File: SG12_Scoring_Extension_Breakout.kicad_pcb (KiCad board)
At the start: 2 copper layers, 95 x 55 mm, 23 parts, among them J1 RJ45, J2 Barrel_Jack_MountingPin, J3 Barrel_Jack_MountingPin, J4 Barrel_Jack_MountingPin, J5 Barrel_Jack_MountingPin, J6 Barrel_Jack_MountingPin, J8 Conn_02x08_Odd_Even, Q1 IRF4905, Q2 IRF4905, Q3 IRF4905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

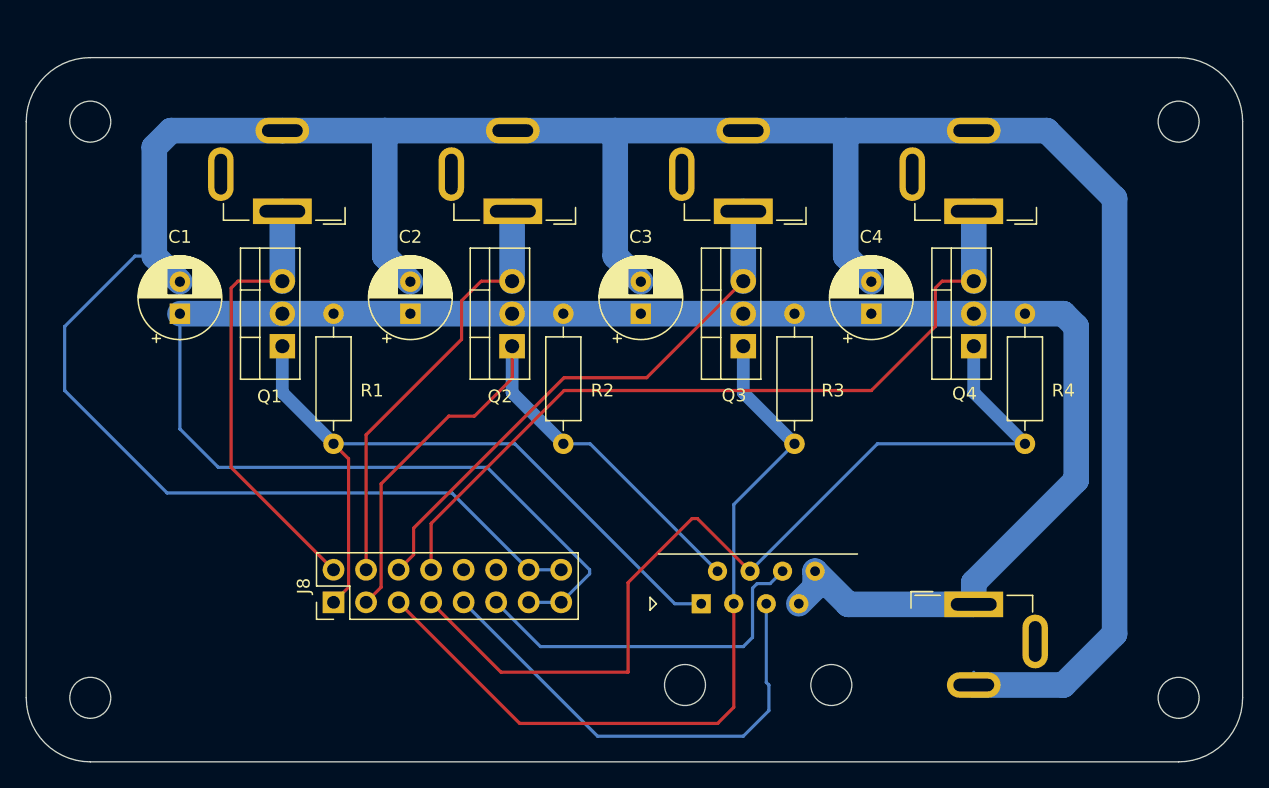
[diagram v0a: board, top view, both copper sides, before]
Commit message: Added silkscreen text
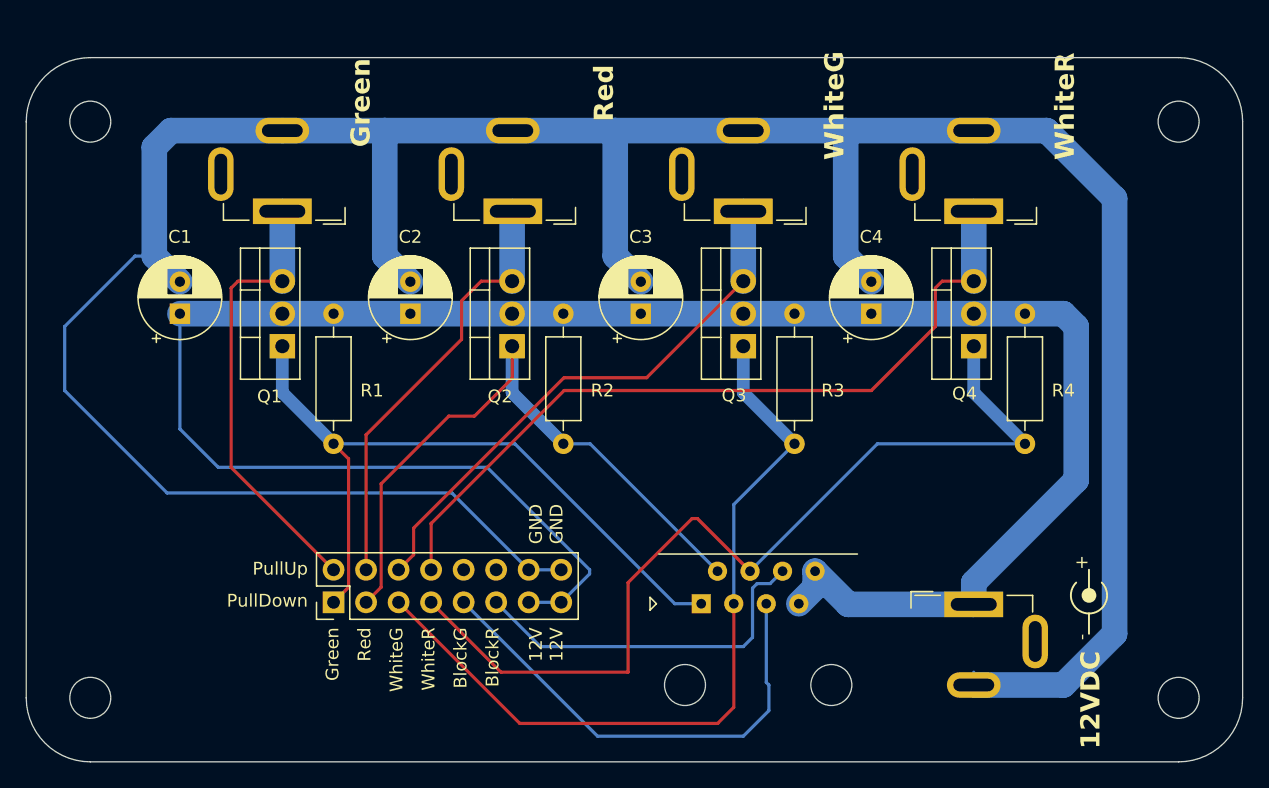
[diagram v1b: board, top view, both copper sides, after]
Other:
- board text added: "+"
- board text added: "-"
- board text added: "12V 12V"
- board text added: "12VDC"
- board text added: "BlockG"
- board text added: "BlockR"
- board text added: "GND GND"
- board text added: "Green"
- board text added: "PullDown"
- board text added: "PullUp"
- board text added: "Red"
- board text added: "WhiteG"
- board text added: "WhiteR"
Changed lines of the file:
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@@
       (outputformat 1)
       (mirror false)
-      (drillshape 1)
+      (drillshape 0)
       (scaleselection 1)
-      (outputdirectory "")
+      (outputdirectory "manufacturing/")
     )
   )
@@
     (property "ki_keywords" "connector")
     (attr through_hole)
-    (fp_text reference "J8" (at 1.27 -2.33 90) (layer "F.SilkS")
+    (fp_text reference "J8" (at 1.27 -2.33 90) (layer "F.SilkS") hide
         (effects (font (size 1 1) (thickness 0.15)))
     )
@@
     (pad "" np_thru_hole circle (at 0 0) (size 3.2 3.2) (drill 3.2) (layers "*.Cu" "*.Mask"))
   )
+  (gr_circle (center 199 120) (end 199.5 120)
+    (stroke (width 0.15) (type solid)) (fill solid) (layer "F.SilkS"))
+  (gr_arc (start 200 119) (mid 199 121.414214) (end 198 119)
+    (stroke (width 0.15) (type default)) (layer "F.SilkS"))
+  (gr_line (start 199 120) (end 199 118)
+    (stroke (width 0.15) (type default)) (layer "F.SilkS"))
+  (gr_line (start 199 121.414214) (end 199 123)
+    (stroke (width 0.15) (type default)) (layer "F.SilkS"))
   (gr_line (start 206 78) (end 121 78)
     (stroke (width 0.1) (type default)) (layer "Edge.Cuts"))
@@
   (gr_arc (start 121 133) (mid 117.464466 131.535534) (end 116 128)
     (stroke (width 0.1) (type default)) (layer "Edge.Cuts"))
+  (gr_text "PullDown" (at 138 121) (layer "F.SilkS")
+    (effects (font (size 1 1) (thickness 0.15)) (justify right bottom))
+  )
+  (gr_text "Red" (at 143 122.5 90) (layer "F.SilkS")
+    (effects (font (size 1 1) (thickness 0.15)) (justify right bottom))
+  )
+  (gr_text "12V\n12V" (at 158 122.5 90) (layer "F.SilkS")
+    (effects (font (size 1 1) (thickness 0.15)) (justify right bottom))
+  )
+  (gr_text "PullUp" (at 138 118.5) (layer "F.SilkS")
+    (effects (font (size 1 1) (thickness 0.15)) (justify right bottom))
+  )
+  (gr_text "+" (at 199 118 90) (layer "F.SilkS")
+    (effects (font (size 1 1) (thickness 0.15)) (justify left bottom))
+  )
+  (gr_text "BlockG" (at 150.5 122.5 90) (layer "F.SilkS")
+    (effects (font (size 1 1) (thickness 0.15)) (justify right bottom))
+  )
+  (gr_text "WhiteR" (at 198 86 90) (layer "F.SilkS")
+    (effects (font (size 1.5 1.5) (thickness 0.3) bold) (justify left bottom))
+  )
+  (gr_text "WhiteG" (at 180 86 90) (layer "F.SilkS")
+    (effects (font (size 1.5 1.5) (thickness 0.3) bold) (justify left bottom))
+  )
+  (gr_text "-" (at 199 123 90) (layer "F.SilkS")
+    (effects (font (size 1 1) (thickness 0.15)) (justify right bottom))
+  )
+  (gr_text "GND\nGND" (at 158 116 90) (layer "F.SilkS")
+    (effects (font (size 1 1) (thickness 0.15)) (justify left bottom))
+  )
+  (gr_text "BlockR" (at 153 122.5 90) (layer "F.SilkS")
+    (effects (font (size 1 1) (thickness 0.15)) (justify right bottom))
+  )
+  (gr_text "WhiteR" (at 148 122.5 90) (layer "F.SilkS")
+    (effects (font (size 1 1) (thickness 0.15)) (justify right bottom))
+  )
+  (gr_text "12VDC" (at 200 132 90) (layer "F.SilkS")
+    (effects (font (size 1.5 1.5) (thickness 0.3) bold) (justify left bottom))
+  )
+  (gr_text "Green" (at 143 85 90) (layer "F.SilkS")
+    (effects (font (size 1.5 1.5) (thickness 0.3) bold) (justify left bottom))
+  )
+  (gr_text "Red" (at 162 83 90) (layer "F.SilkS")
+    (effects (font (size 1.5 1.5) (thickness 0.3) bold) (justify left bottom))
+  )
+  (gr_text "Green" (at 140.5 122.5 90) (layer "F.SilkS")
+    (effects (font (size 1 1) (thickness 0.15)) (justify right bottom))
+  )
+  (gr_text "WhiteG" (at 145.5 122.5 90) (layer "F.SilkS")
+    (effects (font (size 1 1) (thickness 0.15)) (justify right bottom))
+  )
   (segment (start 141.175 109.335) (end 140 108.16) (width 0.25) (layer "F.Cu") (net 1))
   (segment (start 141.175 119.365) (end 141.175 109.335) (width 0.25) (layer "F.Cu") (net 1))

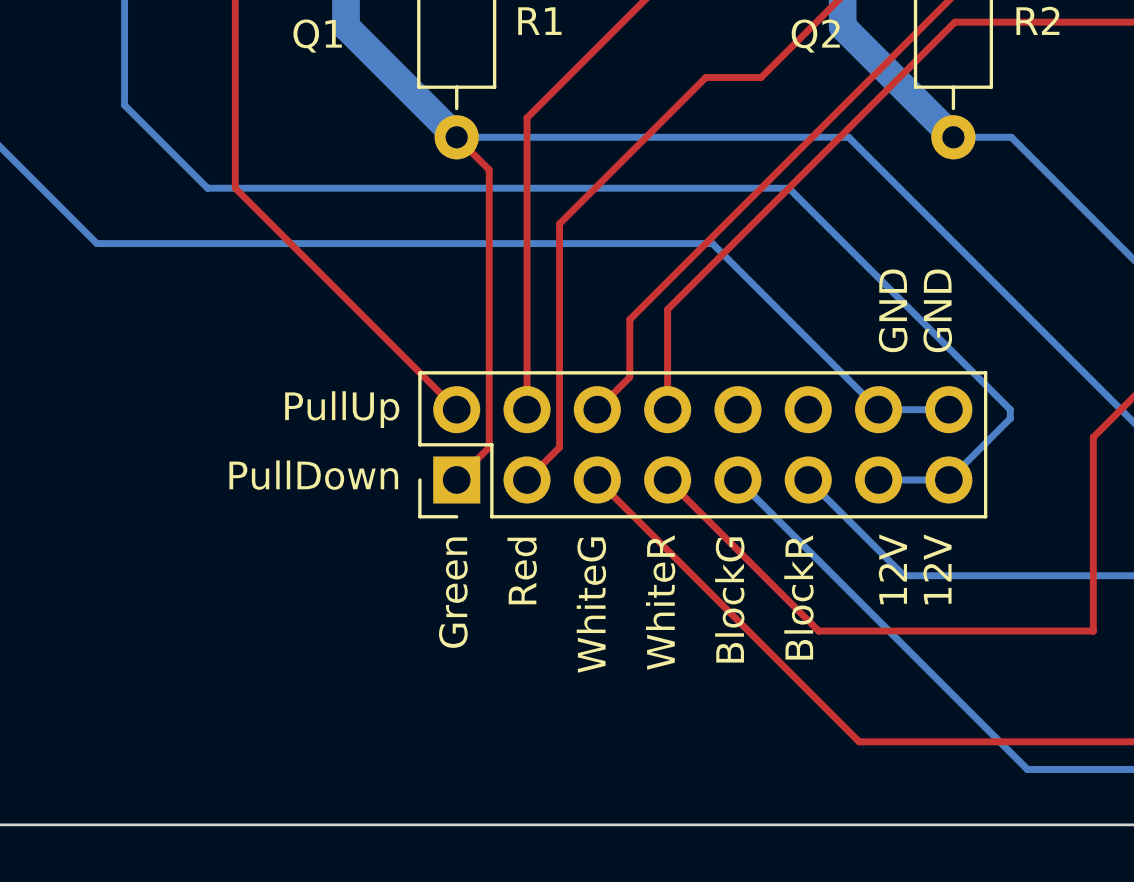
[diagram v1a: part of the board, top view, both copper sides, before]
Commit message: More silkscreen
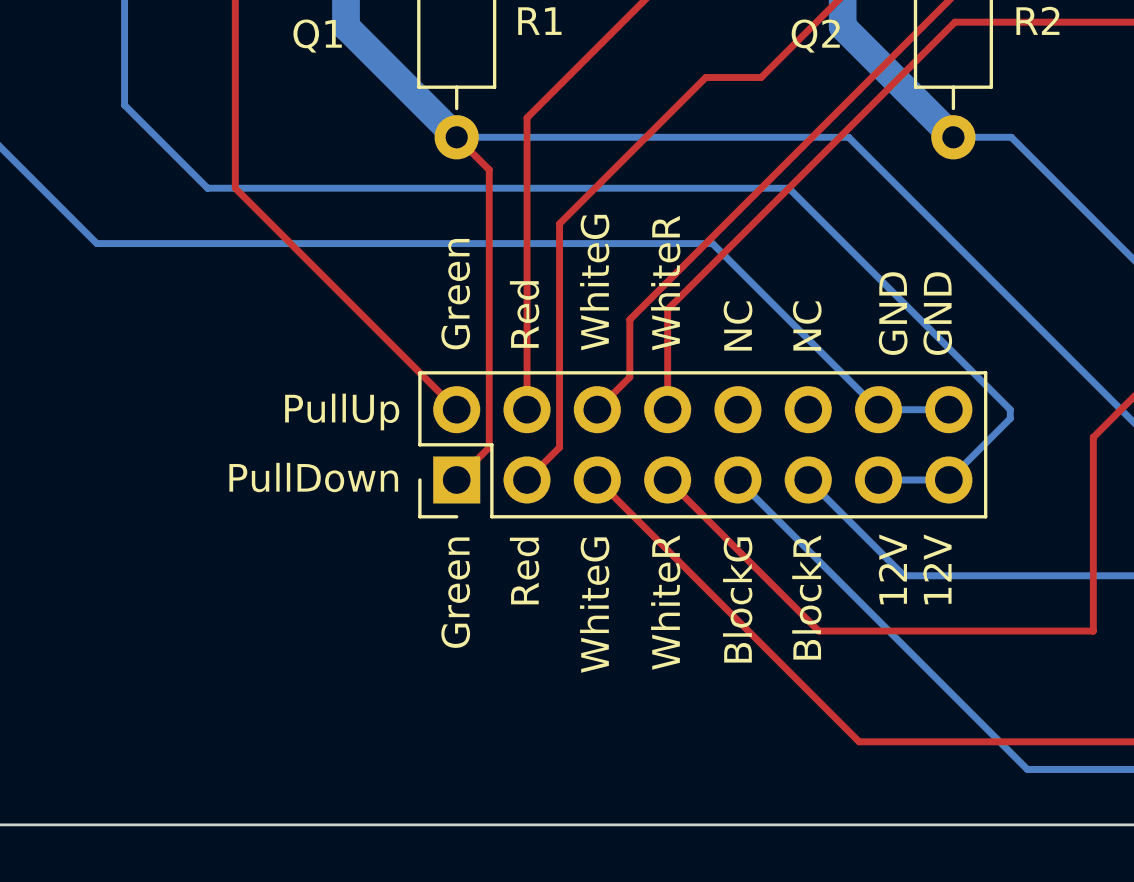
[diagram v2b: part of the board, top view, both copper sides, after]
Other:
- board text added: "NC"
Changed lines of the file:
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@@
   (gr_arc (start 121 133) (mid 117.464466 131.535534) (end 116 128)
     (stroke (width 0.1) (type default)) (layer "Edge.Cuts"))
-  (gr_text "PullDown" (at 138 121) (layer "F.SilkS")
-    (effects (font (size 1 1) (thickness 0.15)) (justify right bottom))
+  (gr_text "NC" (at 150.2 116 90) (layer "F.SilkS")
+    (effects (font (size 1 1) (thickness 0.15)) (justify left))
   )
-  (gr_text "Red" (at 143 122.5 90) (layer "F.SilkS")
-    (effects (font (size 1 1) (thickness 0.15)) (justify right bottom))
+  (gr_text "WhiteG" (at 145.034 115.9 90) (layer "F.SilkS")
+    (effects (font (size 1 1) (thickness 0.15)) (justify left))
+  )
+  (gr_text "PullDown" (at 138 120.5) (layer "F.SilkS")
+    (effects (font (size 1 1) (thickness 0.15)) (justify right))
+  )
+  (gr_text "NC" (at 152.7 116 90) (layer "F.SilkS")
+    (effects (font (size 1 1) (thickness 0.15)) (justify left))
+  )
+  (gr_text "Red" (at 142.5 122.5 90) (layer "F.SilkS")
+    (effects (font (size 1 1) (thickness 0.15)) (justify right))
   )
   (gr_text "12V\n12V" (at 158 122.5 90) (layer "F.SilkS")
     (effects (font (size 1 1) (thickness 0.15)) (justify right bottom))
   )
-  (gr_text "PullUp" (at 138 118.5) (layer "F.SilkS")
-    (effects (font (size 1 1) (thickness 0.15)) (justify right bottom))
+  (gr_text "PullUp" (at 138 118) (layer "F.SilkS")
+    (effects (font (size 1 1) (thickness 0.15)) (justify right))
   )
   (gr_text "+" (at 199 118 90) (layer "F.SilkS")
     (effects (font (size 1 1) (thickness 0.15)) (justify left bottom))
   )
-  (gr_text "BlockG" (at 150.5 122.5 90) (layer "F.SilkS")
-    (effects (font (size 1 1) (thickness 0.15)) (justify right bottom))
+  (gr_text "BlockG" (at 150.2 122.5 90) (layer "F.SilkS")
+    (effects (font (size 1 1) (thickness 0.15)) (justify right))
   )
   (gr_text "WhiteR" (at 198 86 90) (layer "F.SilkS")
     (effects (font (size 1.5 1.5) (thickness 0.3) bold) (justify left bottom))
+  )
+  (gr_text "Green" (at 140 115.9 90) (layer "F.SilkS")
+    (effects (font (size 1 1) (thickness 0.15)) (justify left))
+  )
+  (gr_text "WhiteR" (at 147.6 115.9 90) (layer "F.SilkS")
+    (effects (font (size 1 1) (thickness 0.15)) (justify left))
   )
   (gr_text "WhiteG" (at 180 86 90) (layer "F.SilkS")
@@
     (effects (font (size 1 1) (thickness 0.15)) (justify right bottom))
   )
-  (gr_text "GND\nGND" (at 158 116 90) (layer "F.SilkS")
+  (gr_text "GND\nGND" (at 158 116.1 90) (layer "F.SilkS")
     (effects (font (size 1 1) (thickness 0.15)) (justify left bottom))
   )
-  (gr_text "BlockR" (at 153 122.5 90) (layer "F.SilkS")
-    (effects (font (size 1 1) (thickness 0.15)) (justify right bottom))
+  (gr_text "BlockR" (at 152.7 122.5 90) (layer "F.SilkS")
+    (effects (font (size 1 1) (thickness 0.15)) (justify right))
   )
-  (gr_text "WhiteR" (at 148 122.5 90) (layer "F.SilkS")
-    (effects (font (size 1 1) (thickness 0.15)) (justify right bottom))
+  (gr_text "Red" (at 142.5 115.9 90) (layer "F.SilkS")
+    (effects (font (size 1 1) (thickness 0.15)) (justify left))
+  )
+  (gr_text "WhiteR" (at 147.6 122.5 90) (layer "F.SilkS")
+    (effects (font (size 1 1) (thickness 0.15)) (justify right))
   )
   (gr_text "12VDC" (at 200 132 90) (layer "F.SilkS")
@@
     (effects (font (size 1.5 1.5) (thickness 0.3) bold) (justify left bottom))
   )
-  (gr_text "Green" (at 140.5 122.5 90) (layer "F.SilkS")
-    (effects (font (size 1 1) (thickness 0.15)) (justify right bottom))
+  (gr_text "Green" (at 140 122.5 90) (layer "F.SilkS")
+    (effects (font (size 1 1) (thickness 0.15)) (justify right))
   )
-  (gr_text "WhiteG" (at 145.5 122.5 90) (layer "F.SilkS")
-    (effects (font (size 1 1) (thickness 0.15)) (justify right bottom))
+  (gr_text "WhiteG" (at 145.034 122.5 90) (layer "F.SilkS")
+    (effects (font (size 1 1) (thickness 0.15)) (justify right))
   )
   (segment (start 141.175 109.335) (end 140 108.16) (width 0.25) (layer "F.Cu") (net 1))

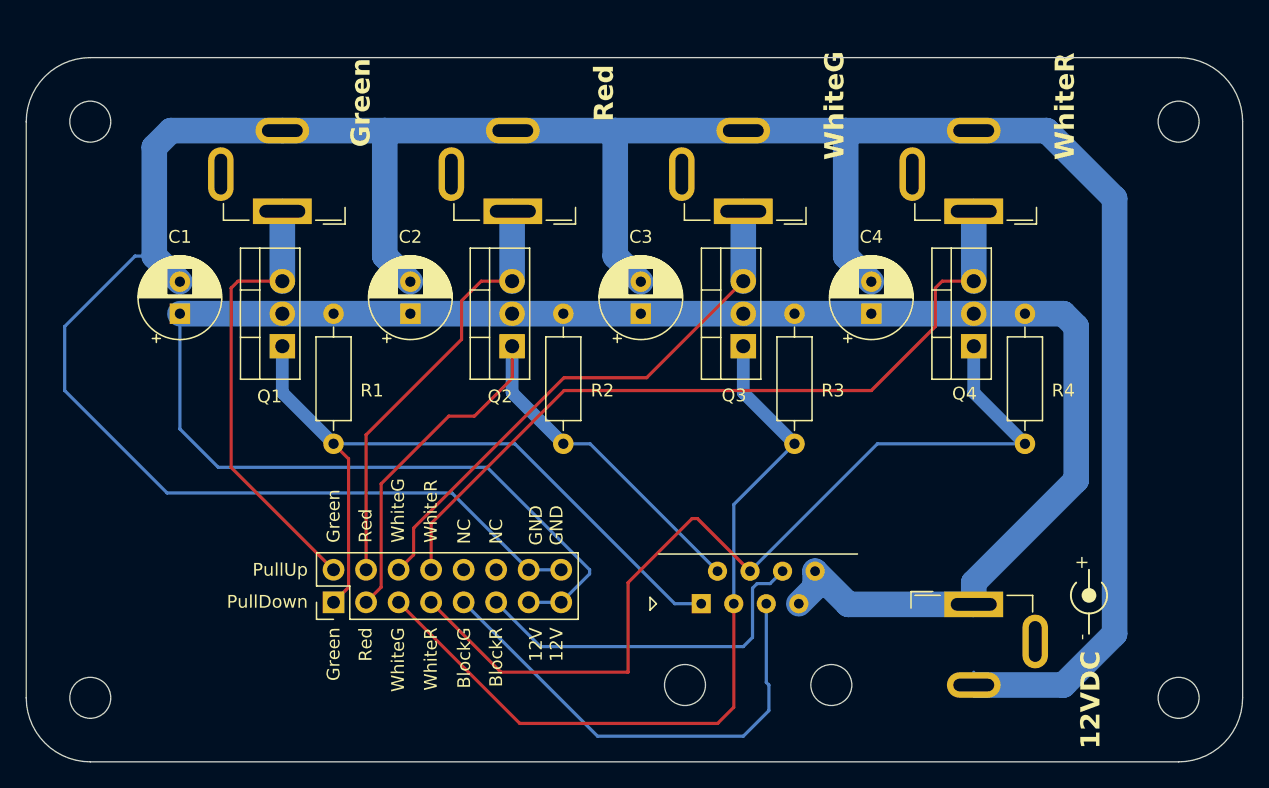
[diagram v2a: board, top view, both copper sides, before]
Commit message: Updated routing and RJ45 footprint
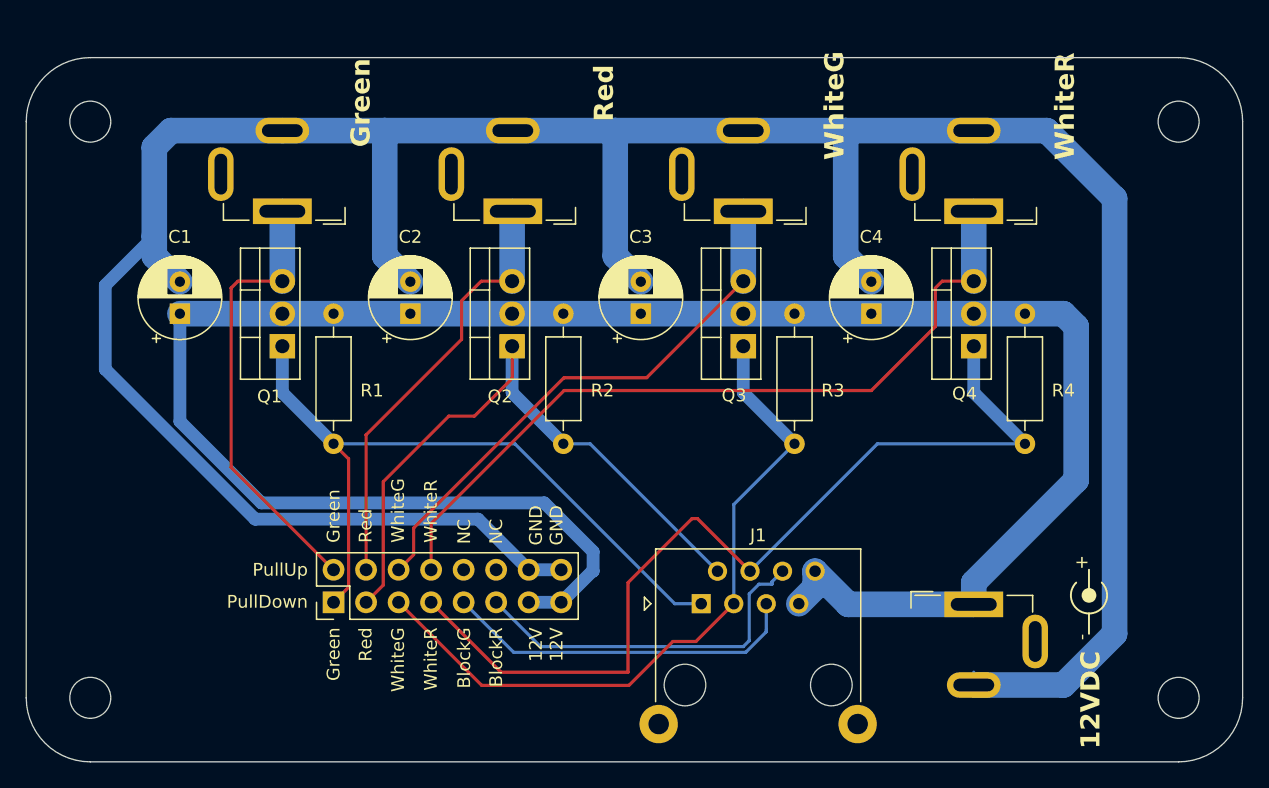
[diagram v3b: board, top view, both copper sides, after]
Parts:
- J1: footprint Connector_RJ:RJ45_Amphenol_54602-x08_Horizontal -> Connector_RJ:RJ45_Ninigi_GE
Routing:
- net Net-(J8-Pin_9): track 37.4 -> 28.1 mm
- net /WhiteG_PullDown: track 62.7 -> 55.5 mm
- net GND: track 233.5 -> 228.7 mm
- net +12V: track 163.5 -> 164.4 mm
